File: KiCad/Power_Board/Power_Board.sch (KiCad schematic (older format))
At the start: 3 parts

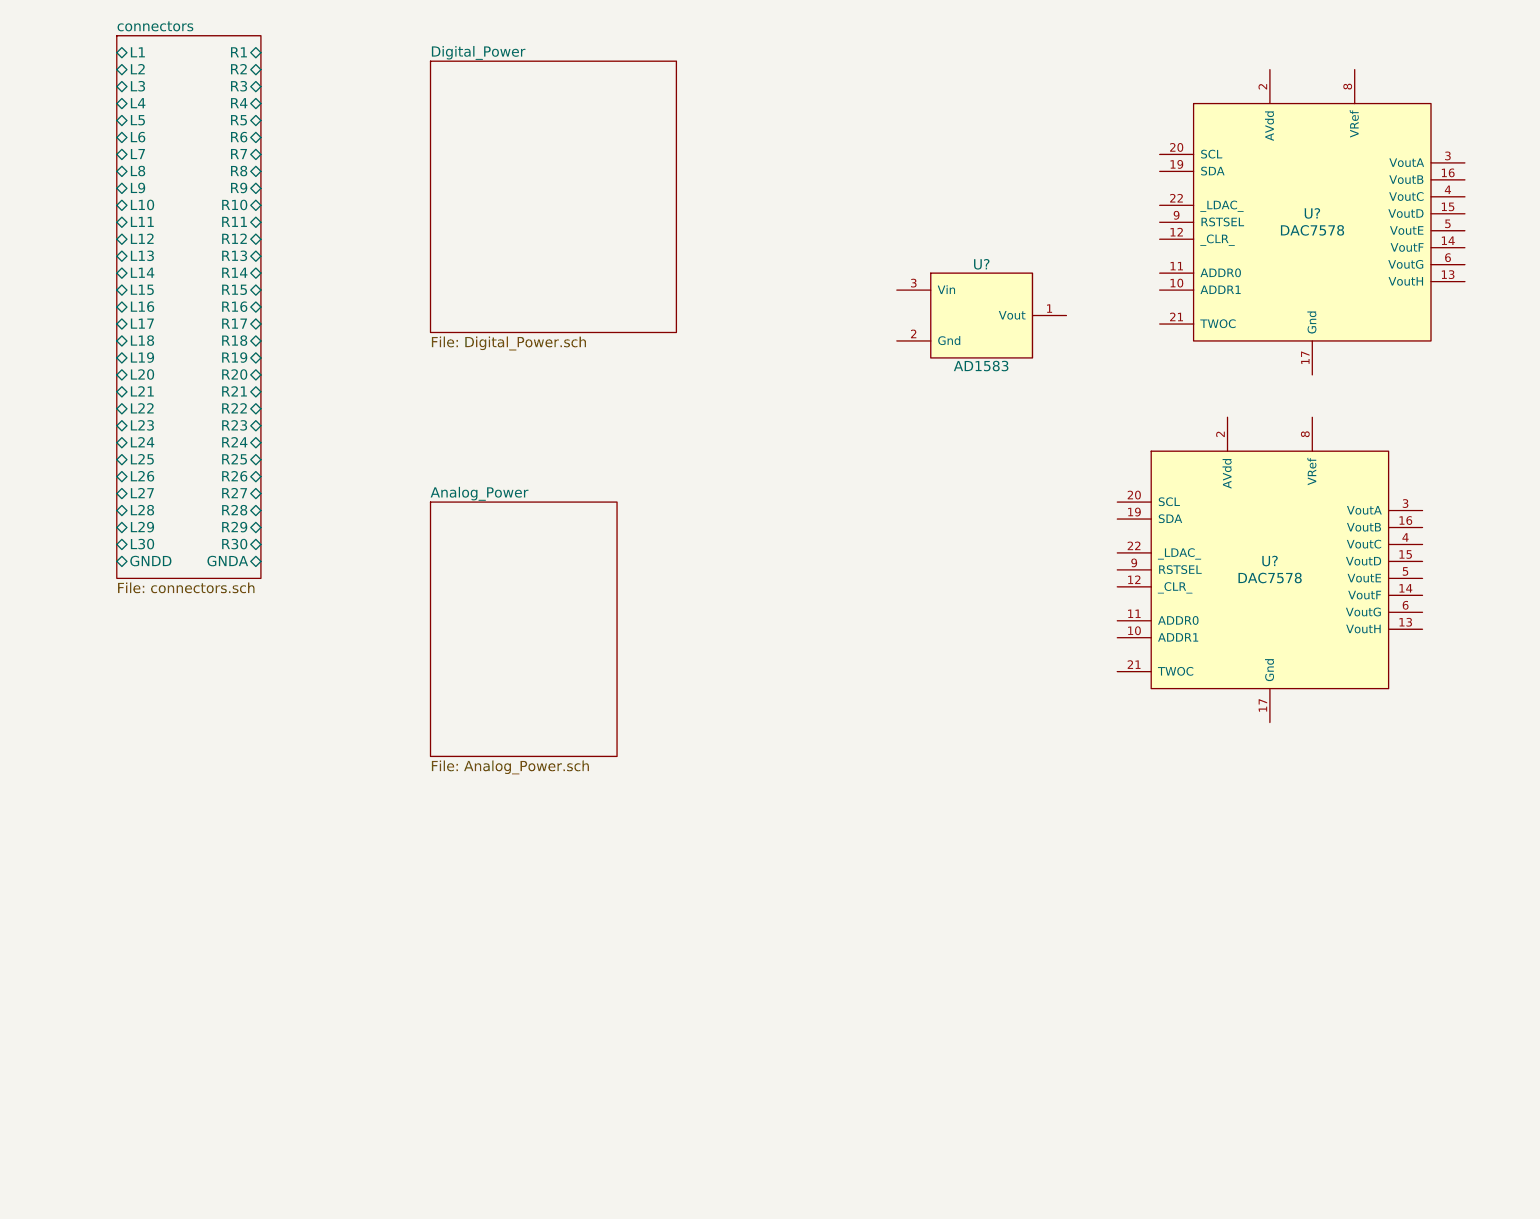
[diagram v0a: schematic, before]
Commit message: Updated power board schematic.
Initial schematic draft. Probably will be modified once layout is
started.
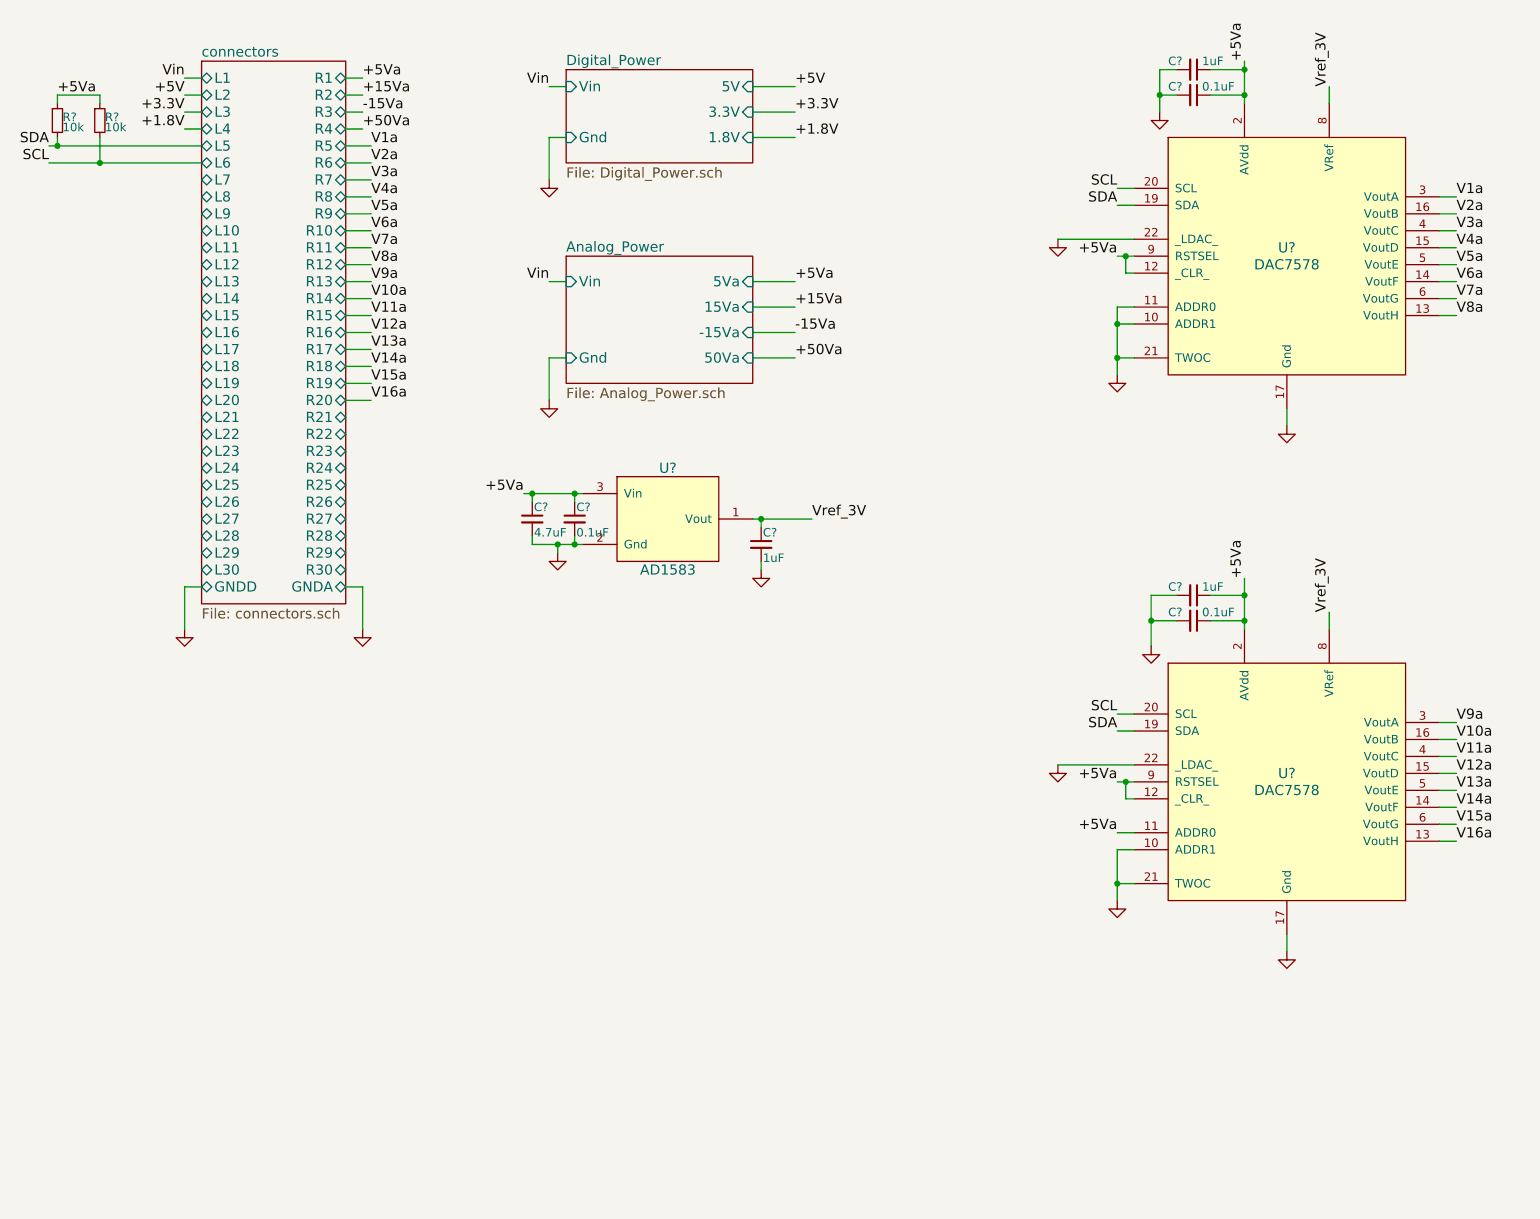
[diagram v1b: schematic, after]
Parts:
- added C? (x3): 0.1uF, symbol C_Small
- added C? (x3): 1uF, symbol C_Small
- added C?: 4.7uF, symbol C_Small
- added R? (x2): 10k, symbol R_Small
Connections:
- net GND: now reaches U?.10 (ADDR1)
- net GND: now also U?.10 (ADDR1), U?.11 (ADDR0), U?.17 (Gnd), U?.17 (Gnd), U?.2 (Gnd), U?.21 (TWOC), U?.21 (TWOC), U?.22 (_LDAC_), U?.22 (_LDAC_), C?.2, C?.2, C?.2, C?.2, C?.2, C?.2, C?.2
- net +5Va: now reaches U?.12 (_CLR_)
- net +5Va: now also U?.11 (ADDR0), U?.12 (_CLR_), U?.2 (AVdd), U?.2 (AVdd), U?.3 (Vin), U?.9 (RSTSEL), U?.9 (RSTSEL), C?.1, C?.1, C?.1, C?.1, C?.1, C?.1, R?.1, R?.1
- net V8a: now reaches U?.13 (VoutH)
- net V6a: now reaches U?.14 (VoutF)
- net V4a: now reaches U?.15 (VoutD)
- net V2a: now reaches U?.16 (VoutB)
- net SDA: now reaches U?.19 (SDA)
- net SDA: now also U?.19 (SDA), R?.2
- net SCL: now reaches U?.20 (SCL)
- net SCL: now also U?.20 (SCL), R?.2
- net V1a: now reaches U?.3 (VoutA)
- net V3a: now reaches U?.4 (VoutC)
- net V5a: now reaches U?.5 (VoutE)
- net V7a: now reaches U?.6 (VoutG)
- net Vref_3V: now reaches U?.8 (VRef)
- net Vref_3V: now also U?.1 (Vout), U?.8 (VRef), C?.1
- net V16a: now reaches U?.13 (VoutH)
- net V14a: now reaches U?.14 (VoutF)
- net V12a: now reaches U?.15 (VoutD)
- net V10a: now reaches U?.16 (VoutB)
- net V9a: now reaches U?.3 (VoutA)
- net V11a: now reaches U?.4 (VoutC)
- net V13a: now reaches U?.5 (VoutE)
- net V15a: now reaches U?.6 (VoutG)
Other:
- moved on the sheet: U?

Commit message: Power board fixes & Updated BOM
Initialized refdes.

Added test clip test points to all power lines (except DACs).

Fixed a feedback resistor mess up on the +/-15V LDOs.
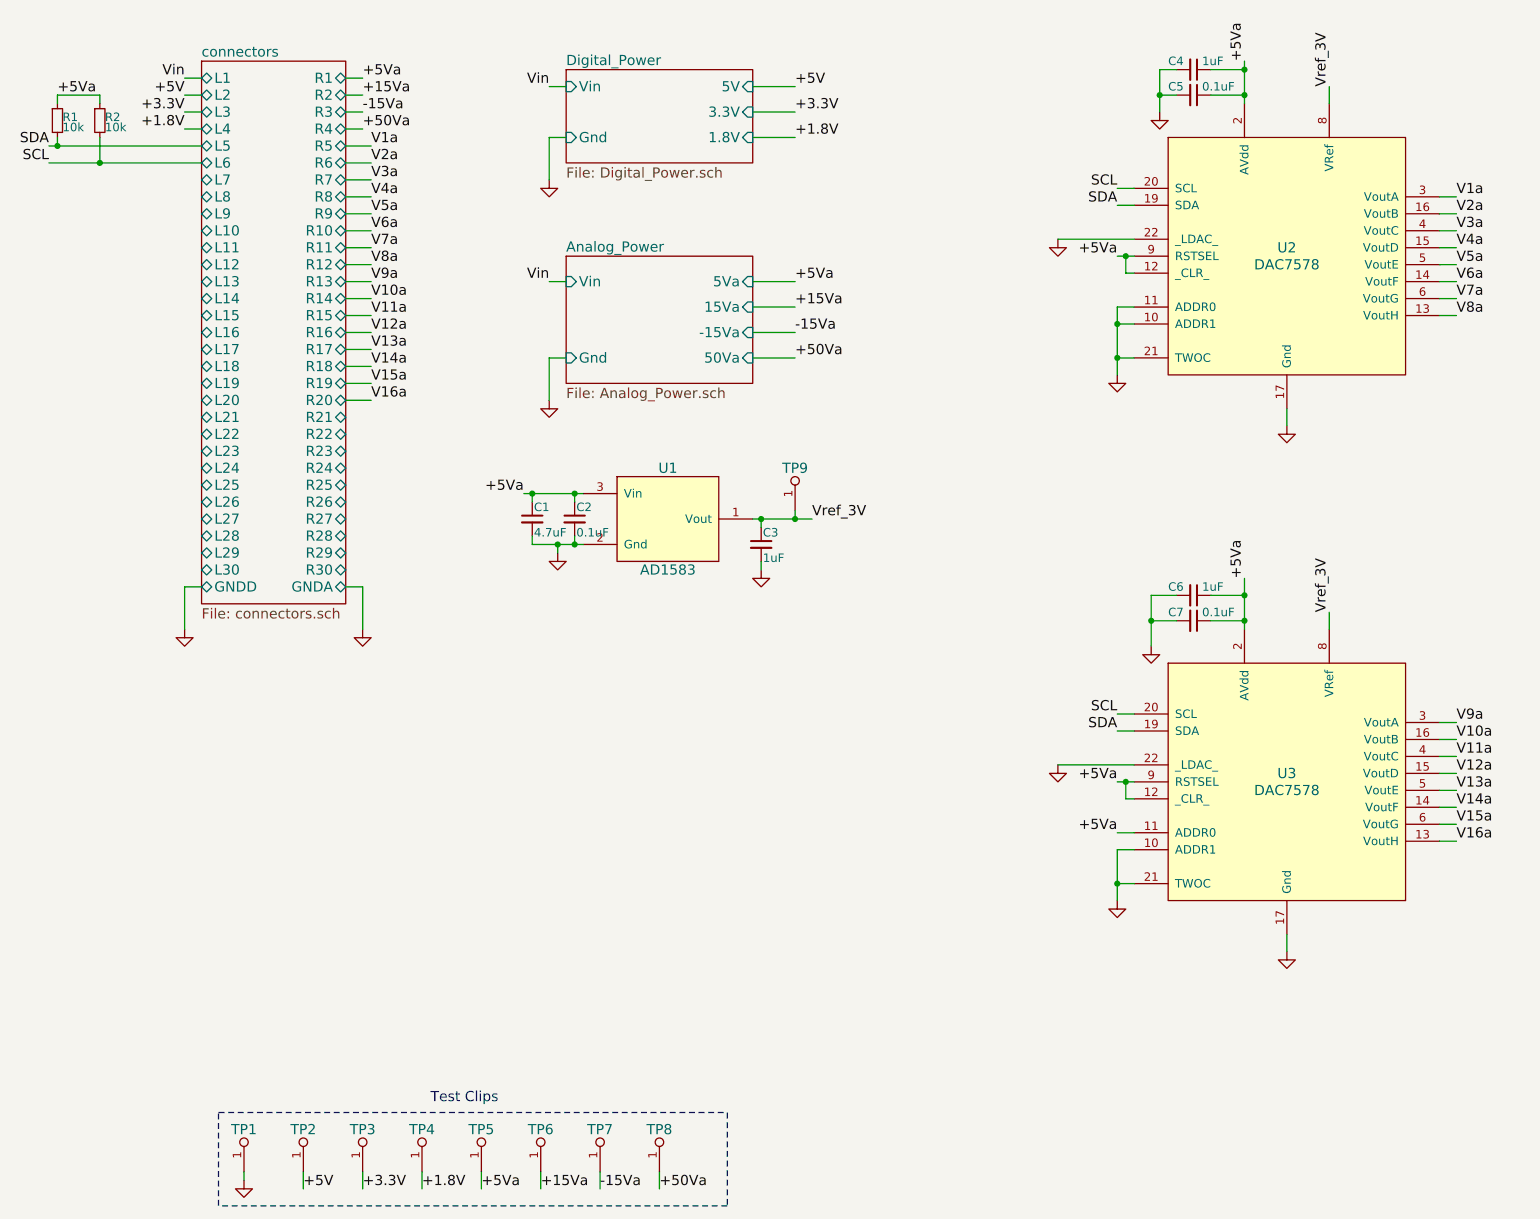
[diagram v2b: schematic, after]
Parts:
- added TP1, TP2, TP3, TP4, TP5, TP6, TP7, TP8, TP9: Test_Point, symbol Test_Point
- gave numbers to parts that had none: 12
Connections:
- net +1.8V: now also TP4.1
- net +15Va: now also TP6.1
- net +3.3V: now also TP3.1
- net +50Va: now also TP8.1
- net +5V: now also TP2.1
- net +5Va: now also TP5.1
- net -15Va: now also TP7.1
- net GND: now also TP1.1
- net Vref_3V: now also TP9.1
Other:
- note added: "Test Clips"

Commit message: Updated BOM & Schematic
BOM was too high.

Switched to a cheaper 8bit DAC. This will still yield ~0.06V resolution
when gained up to +15V.

Currently leaving power circuits alone, but in the future this could be
better optimized for space and cost. Multichannel buck PMIC would be a
good option to simplify the digital supplies.
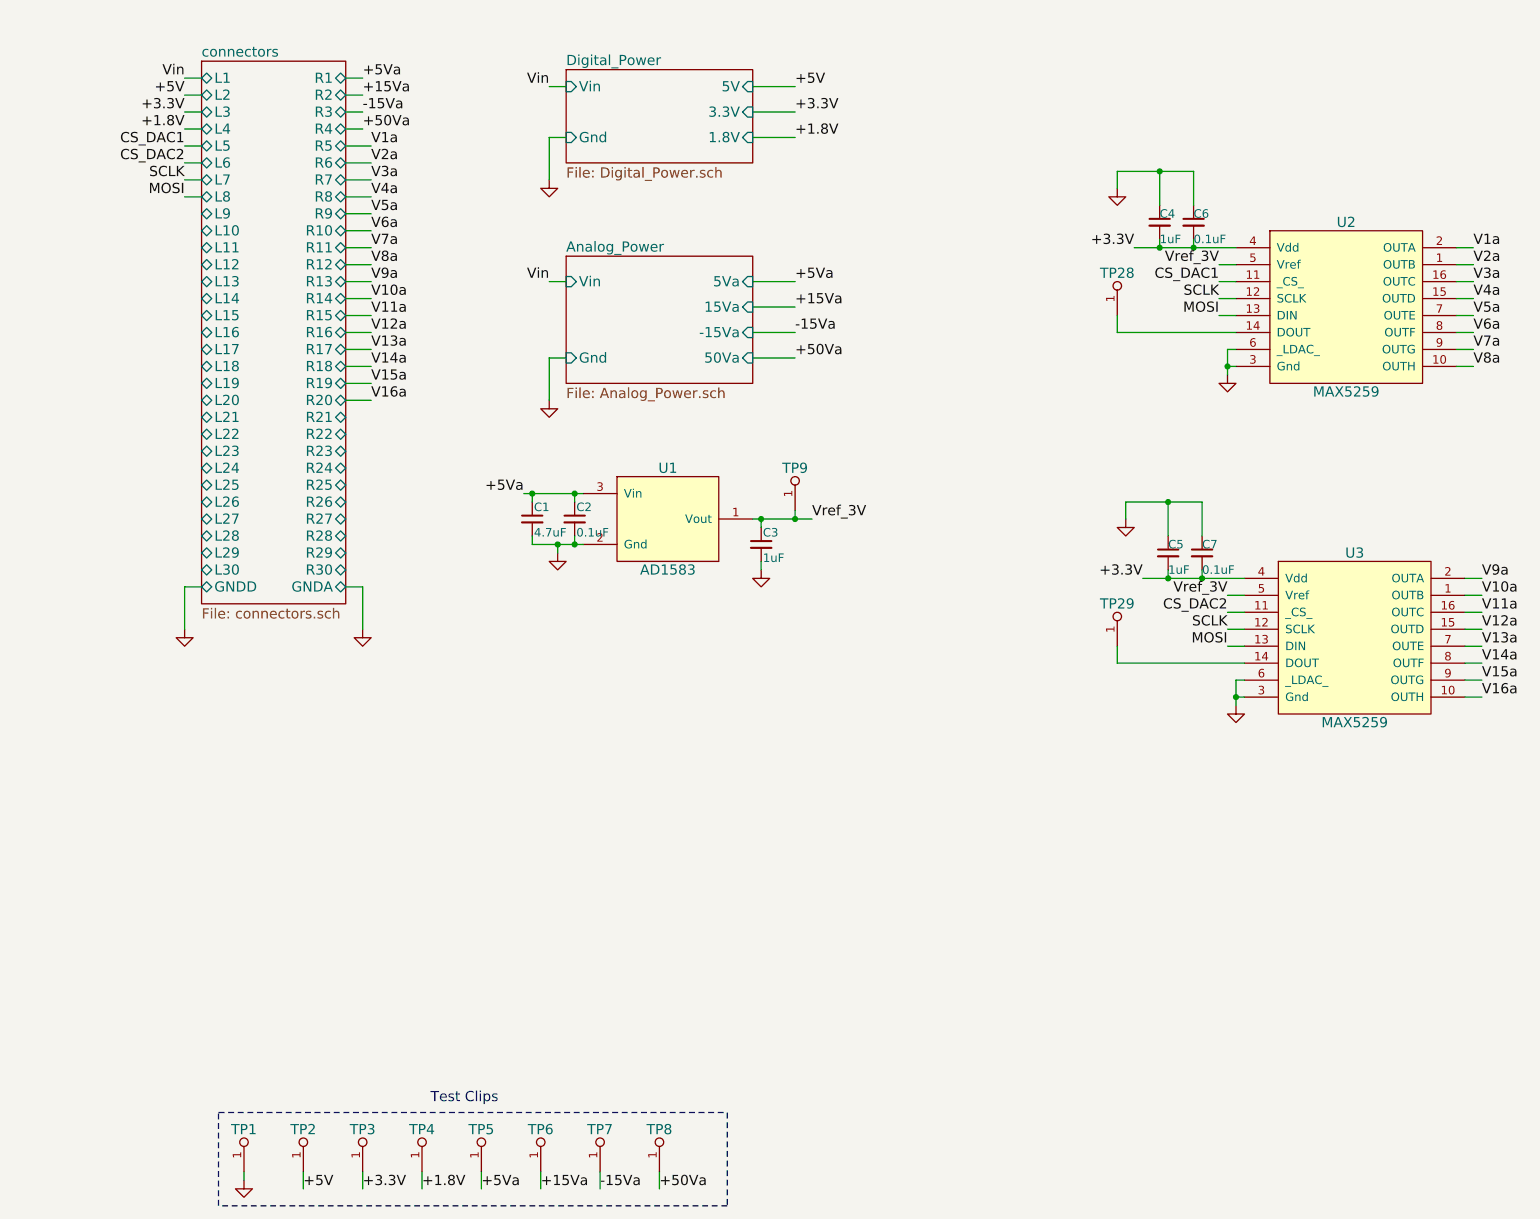
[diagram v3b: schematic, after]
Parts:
- removed R1, R2: 10k, symbol R_Small
- removed U2, U3: DAC7578, symbol DAC7578
- added TP28, TP29: Test_Point, symbol Test_Point
- added U2, U3: MAX5259, symbol MAX5259
- C5: value 0.1uF -> 1uF
- C6: value 1uF -> 0.1uF
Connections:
- net +3.3V: now also C4.2, C5.2, C6.2, C7.2, U2.4 (Vdd), U3.4 (Vdd)
- net +5Va: no longer C4.1, C5.1, C6.1, C7.1
- net GND: now also C4.1, C5.1, C6.1, C7.1, U2.3 (Gnd), U2.6 (_LDAC_), U3.3 (Gnd), U3.6 (_LDAC_); no longer C4.2, C5.2, C6.2, C7.2
- net V10a: now also U3.1 (OUTB)
- net V11a: now also U3.16 (OUTC)
- net V12a: now also U3.15 (OUTD)
- net V13a: now also U3.7 (OUTE)
- net V14a: now also U3.8 (OUTF)
- net V15a: now also U3.9 (OUTG)
- net V16a: now also U3.10 (OUTH)
- net V1a: now also U2.2 (OUTA)
- net V2a: now also U2.1 (OUTB)
- net V3a: now also U2.16 (OUTC)
- net V4a: now also U2.15 (OUTD)
- net V5a: now also U2.7 (OUTE)
- net V6a: now also U2.8 (OUTF)
- net V7a: now also U2.9 (OUTG)
- net V8a: now also U2.10 (OUTH)
- net V9a: now also U3.2 (OUTA)
- net Vref_3V: now also U2.5 (Vref), U3.5 (Vref)
- new net: TP28.1, U2.14 (DOUT)
- new net: TP29.1, U3.14 (DOUT)
- new net CS_DAC1: U2.11 (_CS_)
- new net CS_DAC2: U3.11 (_CS_)
- new net MOSI: U2.13 (DIN), U3.13 (DIN)
- new net SCLK: U2.12 (SCLK), U3.12 (SCLK)
